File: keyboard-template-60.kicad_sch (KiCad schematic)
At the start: 179 parts, among them J1 USB_C_Receptacle_USB2.0, J2 Conn_01x04_MountingPin, J3 AVR-ISP-6, J4 Conn_01x08_Pin, SW1 SW_Reset, U1 ATmega32U4-M, U2 SRV05-4, U3 TP_Sprintek_SK8707-01_Sensor, U6 AMS1117-3.3, Y1 8MHz

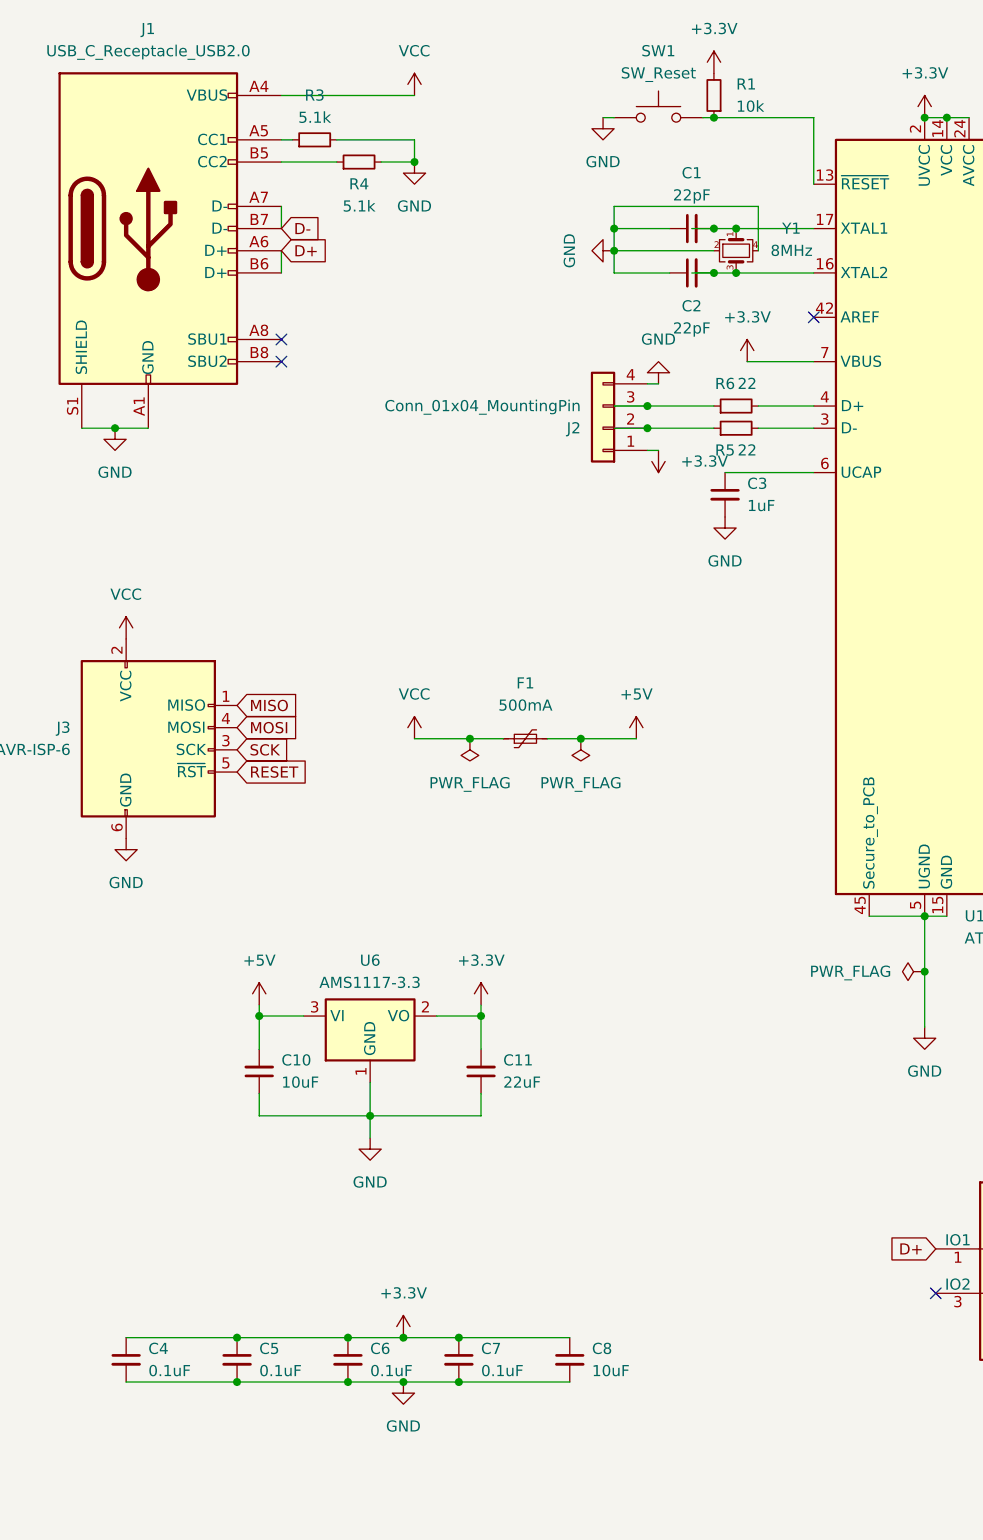
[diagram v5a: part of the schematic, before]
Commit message: Reposition the parts, begin retracing
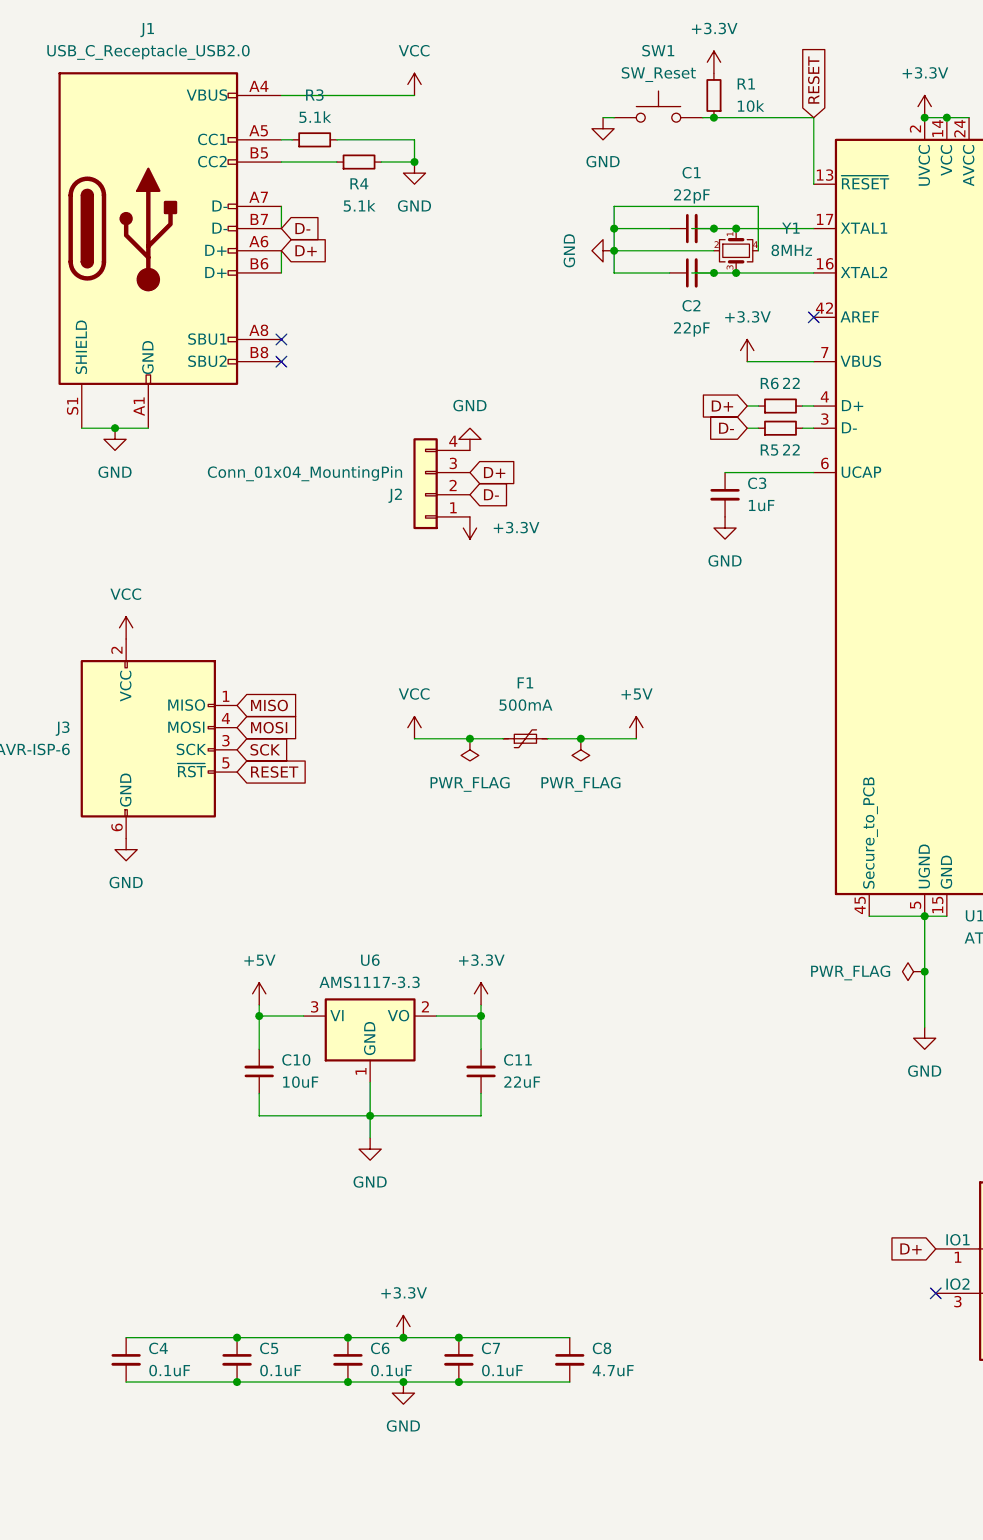
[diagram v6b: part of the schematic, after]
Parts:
- C8: value 10uF -> 4.7uF
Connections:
- net D+: now also J2.3 (Pin_3), R6.1
- net D-: now also J2.2 (Pin_2), R5.1
- net RESET: now also R1.1, SW1.2, U1.13 (~{RESET})
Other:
- moved on the sheet: J2, R5, R6

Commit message: More changes, new footprint, more tracing
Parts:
- added S1, S2: MX_stab, PCM_marbastlib-mx:STAB_MX_2u, symbol PCM_marbastlib-mx:MX_stab
- added S3: MX_stab, PCM_marbastlib-mx:STAB_MX_7u, symbol PCM_marbastlib-mx:MX_stab
- MX67, MX69: footprint MX_Only:MXOnly-2U-Hotswap-ReversedStabilizers -> PCM_marbastlib-mx:SW_MX_HS_CPG151101S11_1u
- MX68: footprint MX_Only:MXOnly-7U-Hotswap -> PCM_marbastlib-mx:SW_MX_HS_CPG151101S11_1u
- U3: footprint ssbb_parts:TP_Sprintek_SK8707-01_Sensor_reversible -> ssbb_parts:TP_Sprintek_SK8707-01-005_Sensor_reversible
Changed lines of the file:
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@@
 	)
 	(symbol
+		(lib_id "PCM_marbastlib-mx:MX_stab")
+		(at 107.95 236.22 0)
+		(unit 1)
+		(exclude_from_sim no)
+		(in_bom yes)
+		(on_board yes)
+		(dnp no)
+		(fields_autoplaced yes)
+		(property "Reference" "S2"
+			(at 114.3 234.8229 0)
+			(effects
+				(font
+					(size 1.27 1.27)
+				)
+				(justify left)
+			)
+		)
+		(property "Value" "MX_stab"
+			(at 114.3 237.3629 0)
+			(effects
+				(font
+					(size 1.27 1.27)
+				)
+				(justify left)
+			)
+		)
+		(property "Footprint" "PCM_marbastlib-mx:STAB_MX_2u"
+			(at 107.95 236.22 0)
+			(effects
+				(font
+					(size 1.27 1.27)
+				)
+				(hide yes)
+			)
+		)
+		(property "Datasheet" ""
+			(at 107.95 236.22 0)
+			(effects
+				(font
+					(size 1.27 1.27)
+				)
+				(hide yes)
+			)
+		)
+		(property "Description" "Cherry MX-style stabilizer"
+			(at 107.95 236.22 0)
+			(effects
+				(font
+					(size 1.27 1.27)
+				)
+				(hide yes)
+			)
+		)
+		(instances
+			(project "keyboard-template-60"
+				(path "/b3baaebd-c99d-4218-99ba-d40a73031965"
+					(reference "S2")
+					(unit 1)
+				)
+			)
+		)
+	)
+	(symbol
 		(lib_id "Device:D_Small")
 		(at 217.17 97.79 90)
@@
 			)
 		)
-		(property "Footprint" "ssbb_parts:TP_Sprintek_SK8707-01_Sensor_reversible"
+		(property "Footprint" "ssbb_parts:TP_Sprintek_SK8707-01-005_Sensor_reversible"
 			(at 279.4 220.98 0)
 			(effects
@@
 			)
 		)
-		(property "Footprint" "MX_Only:MXOnly-2U-Hotswap-ReversedStabilizers"
+		(property "Footprint" "PCM_marbastlib-mx:SW_MX_HS_CPG151101S11_1u"
 			(at 139.065 206.375 0)
 			(effects
@@
 	)
 	(symbol
+		(lib_id "PCM_marbastlib-mx:MX_stab")
+		(at 129.54 236.22 0)
+		(unit 1)
+		(exclude_from_sim no)
+		(in_bom yes)
+		(on_board yes)
+		(dnp no)
+		(fields_autoplaced yes)
+		(property "Reference" "S3"
+			(at 135.89 234.8229 0)
+			(effects
+				(font
+					(size 1.27 1.27)
+				)
+				(justify left)
+			)
+		)
+		(property "Value" "MX_stab"
+			(at 135.89 237.3629 0)
+			(effects
+				(font
+					(size 1.27 1.27)
+				)
+				(justify left)
+			)
+		)
+		(property "Footprint" "PCM_marbastlib-mx:STAB_MX_7u"
+			(at 129.54 236.22 0)
+			(effects
+				(font
+					(size 1.27 1.27)
+				)
+				(hide yes)
+			)
+		)
+		(property "Datasheet" ""
+			(at 129.54 236.22 0)
+			(effects
+				(font
+					(size 1.27 1.27)
+				)
+				(hide yes)
+			)
+		)
+		(property "Description" "Cherry MX-style stabilizer"
+			(at 129.54 236.22 0)
+			(effects
+				(font
+					(size 1.27 1.27)
+				)
+				(hide yes)
+			)
+		)
+		(instances
+			(project "keyboard-template-60"
+				(path "/b3baaebd-c99d-4218-99ba-d40a73031965"
+					(reference "S3")
+					(unit 1)
+				)
+			)
+		)
+	)
+	(symbol
 		(lib_id "Device:D_Small")
 		(at 217.17 135.89 90)
@@
 			)
 		)
-		(property "Footprint" "MX_Only:MXOnly-2U-Hotswap-ReversedStabilizers"
+		(property "Footprint" "PCM_marbastlib-mx:SW_MX_HS_CPG151101S11_1u"
 			(at 113.665 206.375 0)
 			(effects
@@
 			)
 		)
-		(property "Footprint" "MX_Only:MXOnly-7U-Hotswap"
+		(property "Footprint" "PCM_marbastlib-mx:SW_MX_HS_CPG151101S11_1u"
 			(at 126.365 206.375 0)
 			(effects
@@
 					(unit 1)
 				)
+			)
+		)
+	)
+	(symbol
+		(lib_id "PCM_marbastlib-mx:MX_stab")
+		(at 85.09 236.22 0)
+		(unit 1)
+		(exclude_from_sim no)
+		(in_bom yes)
+		(on_board yes)
+		(dnp no)
+		(fields_autoplaced yes)
+		(property "Reference" "S1"
+			(at 91.44 234.8229 0)
+			(effects
+				(font
+					(size 1.27 1.27)
+				)
+				(justify left)
+			)
+		)
+		(property "Value" "MX_stab"
+			(at 91.44 237.3629 0)
+			(effects
+				(font
+					(size 1.27 1.27)
+				)
+				(justify left)
+			)
+		)
+		(property "Footprint" "PCM_marbastlib-mx:STAB_MX_2u"
+			(at 85.09 236.22 0)
+			(effects
+				(font
+					(size 1.27 1.27)
+				)
+				(hide yes)
+			)
+		)
+		(property "Datasheet" ""
+			(at 85.09 236.22 0)
+			(effects
+				(font
+					(size 1.27 1.27)
+				)
+				(hide yes)
+			)
+		)
+		(property "Description" "Cherry MX-style stabilizer"
+			(at 85.09 236.22 0)
+			(effects
+				(font
+					(size 1.27 1.27)
+				)
+				(hide yes)
+			)
+		)
+		(instances
+			(project ""
+				(path "/b3baaebd-c99d-4218-99ba-d40a73031965"
+					(reference "S1")
+					(unit 1)
+				)

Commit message: Updates based on the 008
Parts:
- added U4: SK8707-01, ssbb_parts:TP_Sprintek_SK8707-01_reversible, symbol ssbb_parts:TP_Sprintek_SK8707–01
- U3: footprint ssbb_parts:TP_Sprintek_SK8707-01-005_Sensor_reversible -> ssbb_parts:TP_Sprintek_SK8707-01-008_Sensor
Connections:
- net at U3.1 (S_VCC): now also U4.9 (S_VCC)
- net at U3.2 (S_GND): now also U4.10 (S_GND)
- net at U3.3 (S_Y): now also U4.11 (S_Y)
- net at U3.4 (S_X): now also U4.12 (S_X)
- no-connect marks 12 -> 8
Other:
- moved on the sheet: U3
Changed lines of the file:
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@@
 	)
 	(no_connect
-		(at 287.02 219.71)
-	)
-	(no_connect
-		(at 287.02 217.17)
-	)
-	(no_connect
 		(at 358.14 173.99)
 	)
@@
 	)
 	(no_connect
-		(at 287.02 222.25)
-	)
-	(no_connect
 		(at 283.21 67.31)
 	)
@@
 	)
 	(no_connect
-		(at 287.02 224.79)
-	)
-	(no_connect
 		(at 316.23 226.06)
 	)
@@
 	(wire
 		(pts
+			(xy 261.62 231.14) (xy 271.78 231.14)
+		)
+		(stroke
+			(width 0)
+			(type default)
+		)
+	)
+	(wire
+		(pts
 			(xy 115.57 176.53) (xy 128.27 176.53)
 		)
@@
 	(wire
 		(pts
+			(xy 304.8 223.52) (xy 299.72 223.52)
+		)
+		(stroke
+			(width 0)
+			(type default)
+		)
+	)
+	(wire
+		(pts
 			(xy 234.95 166.37) (xy 234.95 204.47)
 		)
@@
 	(wire
 		(pts
+			(xy 261.62 223.52) (xy 271.78 223.52)
+		)
+		(stroke
+			(width 0)
+			(type default)
+		)
+	)
+	(wire
+		(pts
 			(xy 102.87 62.23) (xy 90.17 62.23)
 		)
@@
 	(wire
 		(pts
+			(xy 261.62 226.06) (xy 271.78 226.06)
+		)
+		(stroke
+			(width 0)
+			(type default)
+		)
+	)
+	(wire
+		(pts
 			(xy 294.64 44.45) (xy 298.45 44.45)
 		)
@@
 	(wire
 		(pts
+			(xy 311.15 215.9) (xy 304.8 215.9)
+		)
+		(stroke
+			(width 0)
+			(type default)
+		)
+	)
+	(wire
+		(pts
 			(xy 234.95 38.1) (xy 234.95 52.07)
 		)
@@
 	(wire
 		(pts
+			(xy 304.8 215.9) (xy 304.8 223.52)
+		)
+		(stroke
+			(width 0)
+			(type default)
+		)
+	)
+	(wire
+		(pts
 			(xy 321.31 49.53) (xy 321.31 52.07)
 		)
@@
 	(wire
 		(pts
+			(xy 299.72 213.36) (xy 311.15 213.36)
+		)
+		(stroke
+			(width 0)
+			(type default)
+		)
+	)
+	(wire
+		(pts
 			(xy 280.67 153.67) (xy 280.67 151.13)
 		)
@@
 	(wire
 		(pts
+			(xy 261.62 228.6) (xy 271.78 228.6)
+		)
+		(stroke
+			(width 0)
+			(type default)
+		)
+	)
+	(wire
+		(pts
 			(xy 323.85 218.44) (xy 323.85 231.14)
 		)
@@
 	(symbol
 		(lib_id "ssbb_parts:TP_Sprintek_SK8707-01_Sensor")
-		(at 279.4 220.98 0)
+		(at 254 227.33 0)
 		(unit 1)
 		(exclude_from_sim no)
@@
 		(fields_autoplaced yes)
 		(property "Reference" "U3"
-			(at 279.4 209.55 0)
+			(at 254 215.9 0)
 			(effects
 				(font
@@
 		)
 		(property "Value" "TP_Sprintek_SK8707-01_Sensor"
-			(at 279.4 212.09 0)
+			(at 254 218.44 0)
 			(effects
 				(font
@@
 			)
 		)
-		(property "Footprint" "ssbb_parts:TP_Sprintek_SK8707-01-005_Sensor_reversible"
-			(at 279.4 220.98 0)
+		(property "Footprint" "ssbb_parts:TP_Sprintek_SK8707-01-008_Sensor"
+			(at 254 227.33 0)
 			(effects
 				(font
@@
 		)
 		(property "Datasheet" ""
-			(at 279.4 220.98 0)
+			(at 254 227.33 0)
 			(effects
 				(font
@@
 		)
 		(property "Description" ""
-			(at 279.4 220.98 0)
+			(at 254 227.33 0)
 			(effects
 				(font
@@
 					(unit 1)
 				)
+			)
+		)
+	)
+	(symbol
+		(lib_id "ssbb_parts:TP_Sprintek_SK8707–01")
+		(at 285.75 222.25 0)
+		(unit 1)
+		(exclude_from_sim no)
+		(in_bom yes)
+		(on_board yes)
+		(dnp no)
+		(fields_autoplaced yes)
+		(property "Reference" "U4"
+			(at 285.75 205.74 0)
+			(effects
+				(font
+					(size 1.27 1.27)
+				)
+			)
+		)
+		(property "Value" "SK8707-01"
+			(at 285.75 208.28 0)
+			(effects
+				(font
+					(size 1.27 1.27)
+				)
+			)
+		)
+		(property "Footprint" "ssbb_parts:TP_Sprintek_SK8707-01_reversible"
+			(at 285.75 222.25 0)
+			(effects
+				(font
+					(size 1.27 1.27)
+				)
+				(hide yes)
+			)
+		)
+		(property "Datasheet" ""
+			(at 285.75 222.25 0)
+			(effects
+				(font
+					(size 1.27 1.27)
+				)
+				(hide yes)
+			)
+		)
+		(property "Description" ""
+			(at 285.75 222.25 0)
+			(effects
+				(font
+					(size 1.27 1.27)
+				)
+				(hide yes)
+			)
+		)
+		(pin "1"
+		)
+		(pin "4"
+		)
+		(pin "12"
+		)
+		(pin "6"
+		)
+		(pin "5"
+		)
+		(pin "2"
+		)
+		(pin "3"
+		)
+		(pin "11"
+		)
+		(pin "10"
+		)
+		(pin "9"
+		)
+		(pin "7"
+		)
+		(pin "8"
+		)
+		(instances
+			(project ""
+				(path "/b3baaebd-c99d-4218-99ba-d40a73031965"
+					(reference "U4")
+					(unit 1)
+				)
